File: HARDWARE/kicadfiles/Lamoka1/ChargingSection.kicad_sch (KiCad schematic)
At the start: 1 part, among them U1 BQ25756RRVR

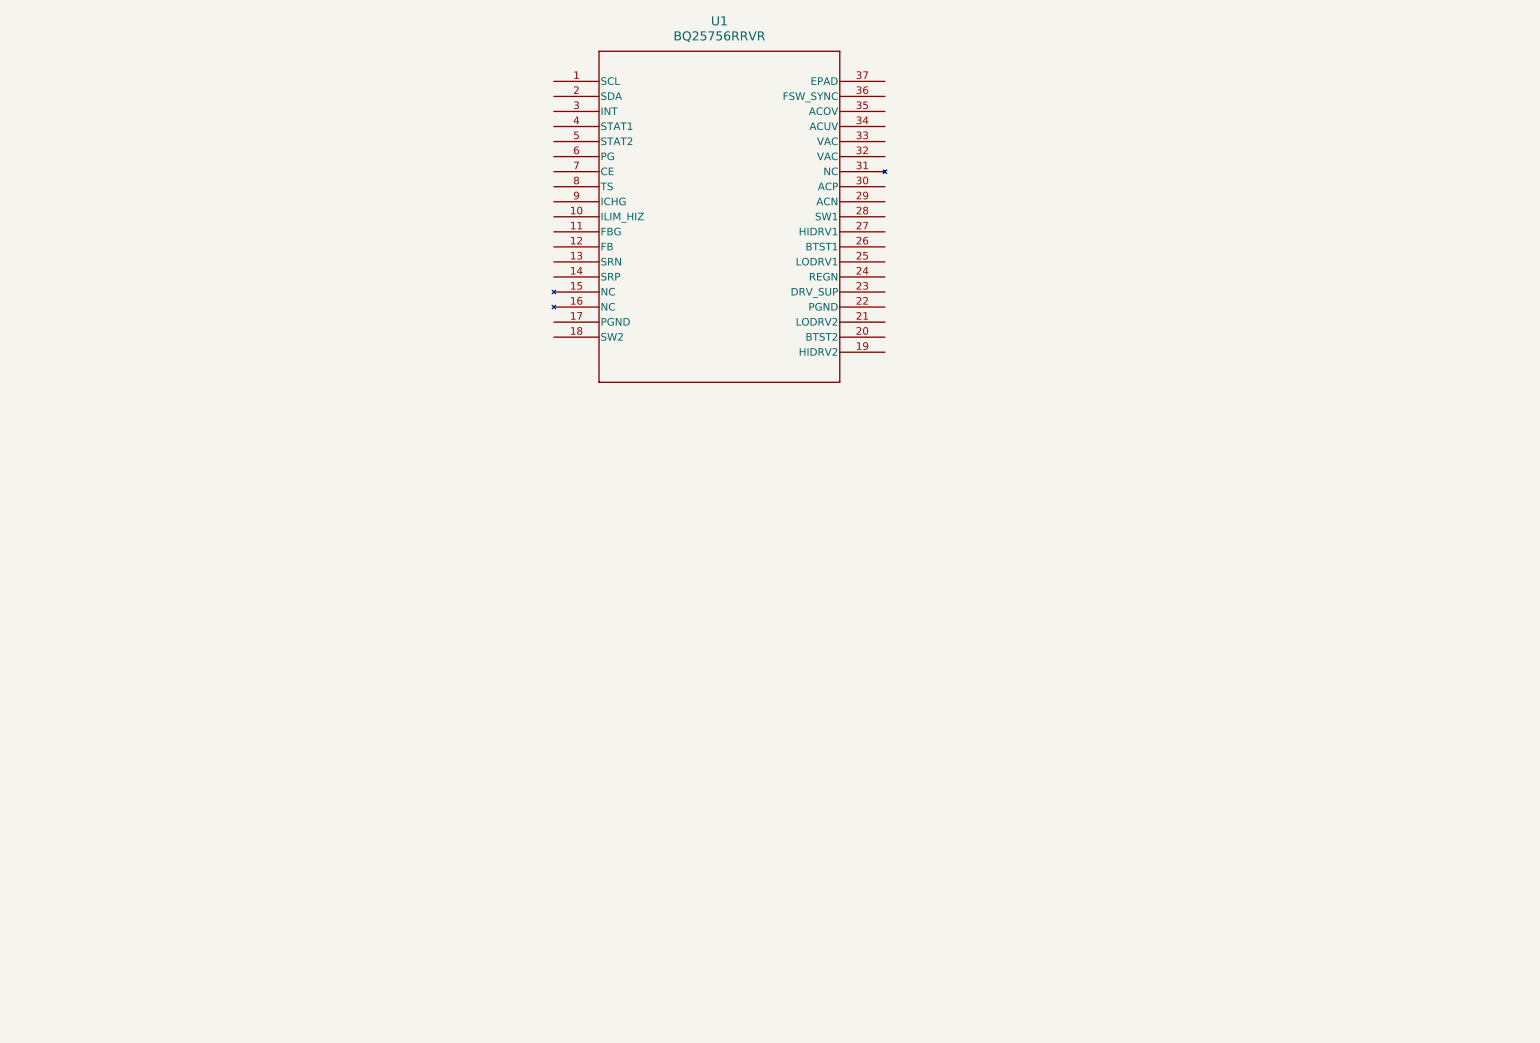
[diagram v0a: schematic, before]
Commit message: ADD charging section and multiple color Dev-Brain 3d print
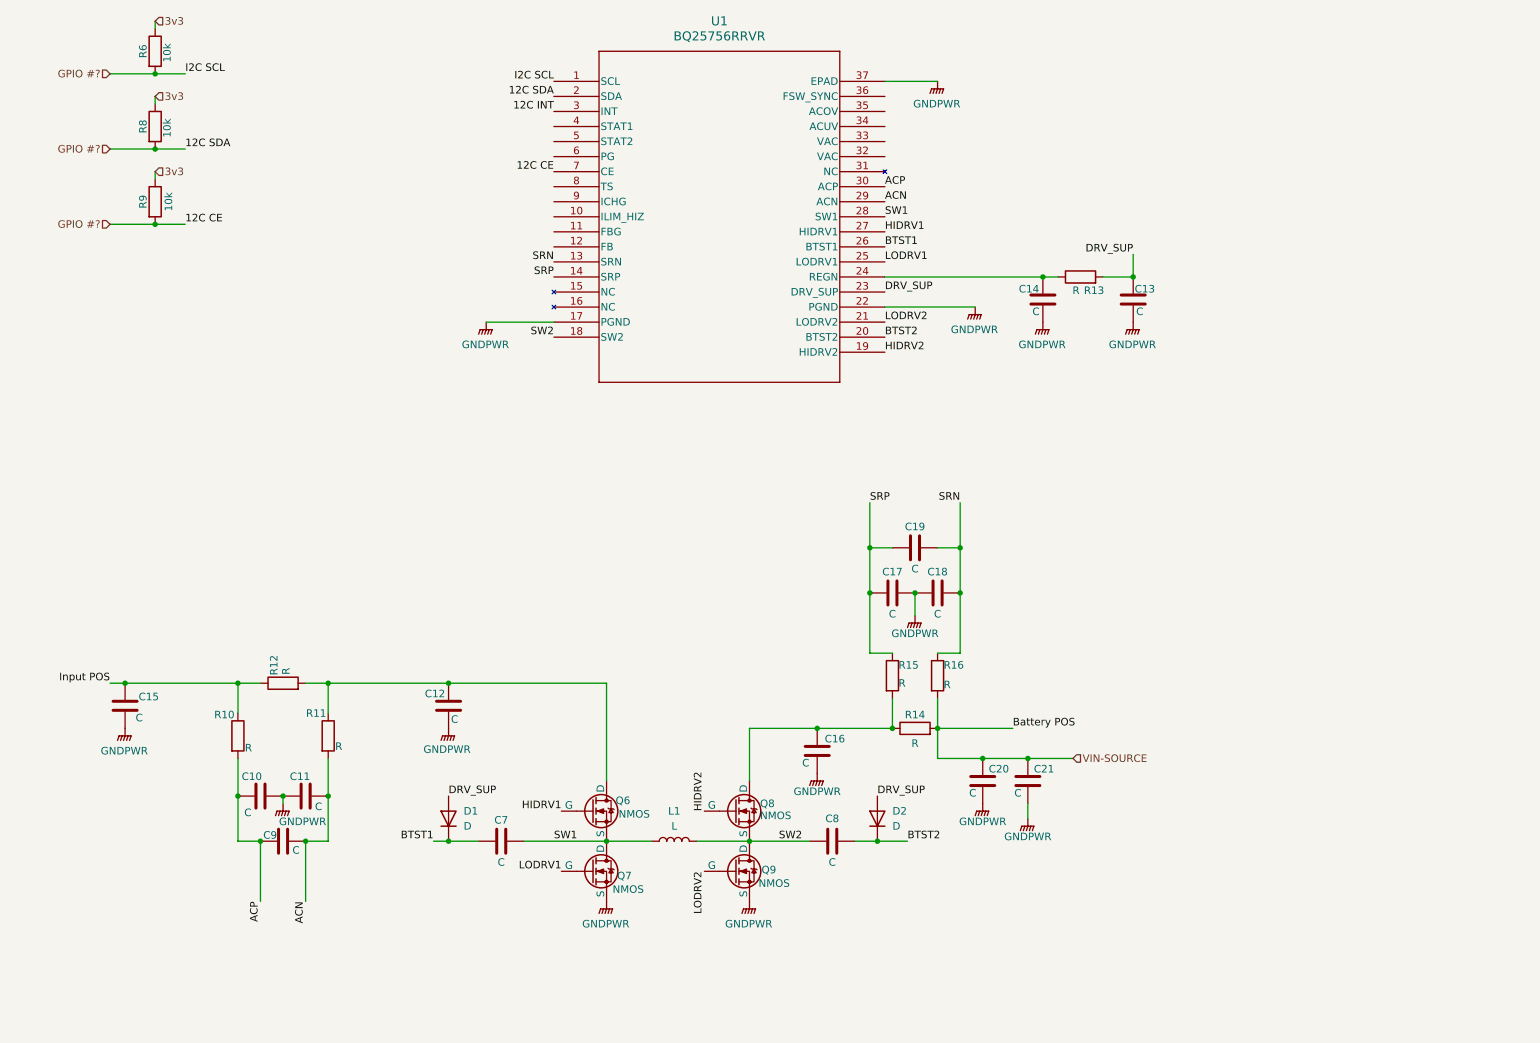
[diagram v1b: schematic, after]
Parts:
- added C10, C11, C12, C13, C14, C15, C16, C17, C18, C19, C20, C21, C7, C8, C9: C, symbol Device:C
- added D1, D2: D, symbol Device:D
- added L1: L, symbol Device:L
- added Q6, Q7, Q8, Q9: NMOS, symbol Simulation_SPICE:NMOS
- added R10, R11, R12, R13, R14, R15, R16: R, symbol Device:R
- added R6, R8, R9: 10k, symbol Device:R
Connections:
- net GPIO #?: now reaches U1.1 (SCL)
- net GPIO #?: now also U1.2 (SDA), U1.7 (CE), R6.2, R8.2, R9.2
- net SRN: now reaches U1.13 (SRN)
- net SRN: now also C18.2, C19.2, R16.1
- net SRP: now reaches U1.14 (SRP)
- net SRP: now also C17.1, C19.1, R15.1
- net GNDPWR: now reaches U1.17 (PGND)
- net GNDPWR: now also U1.22 (PGND), U1.37 (EPAD), C10.2, C11.1, C12.1, C13.2, C14.2, C15.2, C16.2, C17.2, C18.1, C20.2, C21.2, Q7.3 (S), Q9.3 (S)
- net SW2: now reaches U1.18 (SW2)
- net SW2: now also C8.1, L1.2, Q8.3 (S), Q9.1 (D)
- net HIDRV2: now reaches U1.19 (HIDRV2)
- net HIDRV2: now also Q8.2 (G)
- net BTST2: now reaches U1.20 (BTST2)
- net BTST2: now also C8.2, D2.1 (K)
- net LODRV2: now reaches U1.21 (LODRV2)
- net LODRV2: now also Q9.2 (G)
- net DRV_SUP: now reaches U1.23 (DRV_SUP)
- net DRV_SUP: now also C13.1, D1.2 (A), D2.2 (A), R13.2
- net at U1.24 (REGN): now also C14.1, R13.1
- net LODRV1: now reaches U1.25 (LODRV1)
- net LODRV1: now also Q7.2 (G)
- net BTST1: now reaches U1.26 (BTST1)
- net BTST1: now also C7.1, D1.1 (K)
- net HIDRV1: now reaches U1.27 (HIDRV1)
- net HIDRV1: now also Q6.2 (G)
- net SW1: now reaches U1.28 (SW1)
- net SW1: now also C7.2, L1.1, Q6.3 (S), Q7.1 (D)
- net ACN: now reaches U1.29 (ACN)
- net ACN: now also C11.2, C9.2, R11.2
- net 12C INT: now reaches U1.3 (INT)
- net ACP: now reaches U1.30 (ACP)
- net ACP: now also C10.1, C9.1, R10.2
- new net: C12.2, Q6.1 (D), R11.1, R12.2
- new net: C16.1, Q8.1 (D), R14.1, R15.2
- new net 3v3: R6.1, R8.1, R9.1
- new net Input POS: C15.1, R10.1, R12.1
- new net VIN-SOURCE: C20.1, C21.1, R14.2, R16.2

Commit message: ADD better DEV-Brain models, Slight improvements to the Lamoka1 charging section
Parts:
- added C22, C23: C, symbol Device:C
- added R19, R20, R21, R22, R23, R24, R25: R, symbol Device:R
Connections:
- net GNDPWR: now also U1.10 (ILIM_HIZ), U1.9 (ICHG), C22.2, C23.2, R19.2, R22.2
- net Input POS: now also U1.32 (VAC), U1.33 (VAC), C22.1, R20.1, R23.1
- net VIN-SOURCE: now also R24.1
- net FBG: now reaches U1.11 (FBG)
- net FBG: now also R25.2
- net FB: now reaches U1.12 (FB)
- net FB: now also R24.2, R25.1
- net ACUV: now reaches U1.34 (ACUV)
- net ACUV: now also R20.2, R21.1
- net ACOV: now reaches U1.35 (ACOV)
- net ACOV: now also R21.2, R22.1
- net at U1.36 (FSW_SYNC): now also R19.1
- net 12C INT renamed I2C INT
- new net: C23.1, R23.2
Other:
- moved on the sheet: C10, C11, C12, C15, C16, C17, C18, C19, C20, C21, C7, C8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

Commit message: Cleaning the repository
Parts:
- added J2: Conn_01x02_Pin, symbol Connector:Conn_01x02_Pin
- added R17, R18: R, symbol Device:R
- added R26: 10k, symbol Device:R
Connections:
- net I2C INT is gone; now on net GPIO #?: U1.3 (INT)
- net 3v3: now also R26.1
- net GNDPWR: now also J2.2 (Pin_2), R18.2
- net GPIO #?: now also R26.2
- net REGN: now reaches C14.1, R13.1, U1.24 (REGN)
- net REGN: now also R17.1
- net BAT-TEMP-TS: now reaches U1.8 (TS)
- net BAT-TEMP-TS: now also J2.1 (Pin_1), R17.2, R18.1
- no-connect marks 0 -> 3
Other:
- moved on the sheet: C23, R23, R24, R25
